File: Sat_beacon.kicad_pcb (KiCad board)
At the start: 2 copper layers, 8 x 3.6 mm, 127 parts, among them IC1 LMX2581ESQE_NOPB, IC2 LMX2581ESQE_NOPB, J1 Conn_01x05_Pin, J2 Conn_01x05_Pin, J3 Conn_01x03_Pin, J4 MMCX, J5 MMCX, Q1 BC817-40, Q2 BC817-40, Q3 BC817-40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

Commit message: PCB work
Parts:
- removed C50, C59: 4.7u, Capacitor_SMD:C_0805_2012Metric
- moved U5 293.2 mm to (99.8, 151.4), turned to 180 degrees
- moved J5 288.3 mm to (100.8, 160.4), turned to 90 degrees
- moved C65 286.6 mm to (95.3, 145.8), turned to 180 degrees
- moved C66 283.0 mm to (99.1, 148.2), turned to -90 degrees
- moved C67 280.8 mm to (100.8, 148.2), turned to -90 degrees
- moved C68 276.3 mm to (104.4, 145.8)
- moved IC2 274.2 mm to (98.8, 132.1)
- moved R22 266.2 mm to (98.9, 117.9)
- moved R20 255.6 mm to (85.9, 134.7)
- moved C24 255.5 mm to (91.3, 130.3)
- moved C45 255.5 mm to (96.6, 139.2)
- moved C42 255.1 mm to (93.7, 124.3), turned to -90 degrees
- moved C60 252.7 mm to (102.3, 124.5), turned to -90 degrees
- moved R21 252.1 mm to (89.3, 136.7)
- moved C47 242.4 mm to (85.9, 136.7)
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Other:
- board size 8 x 3.6 mm -> 3.6 x 8 mm

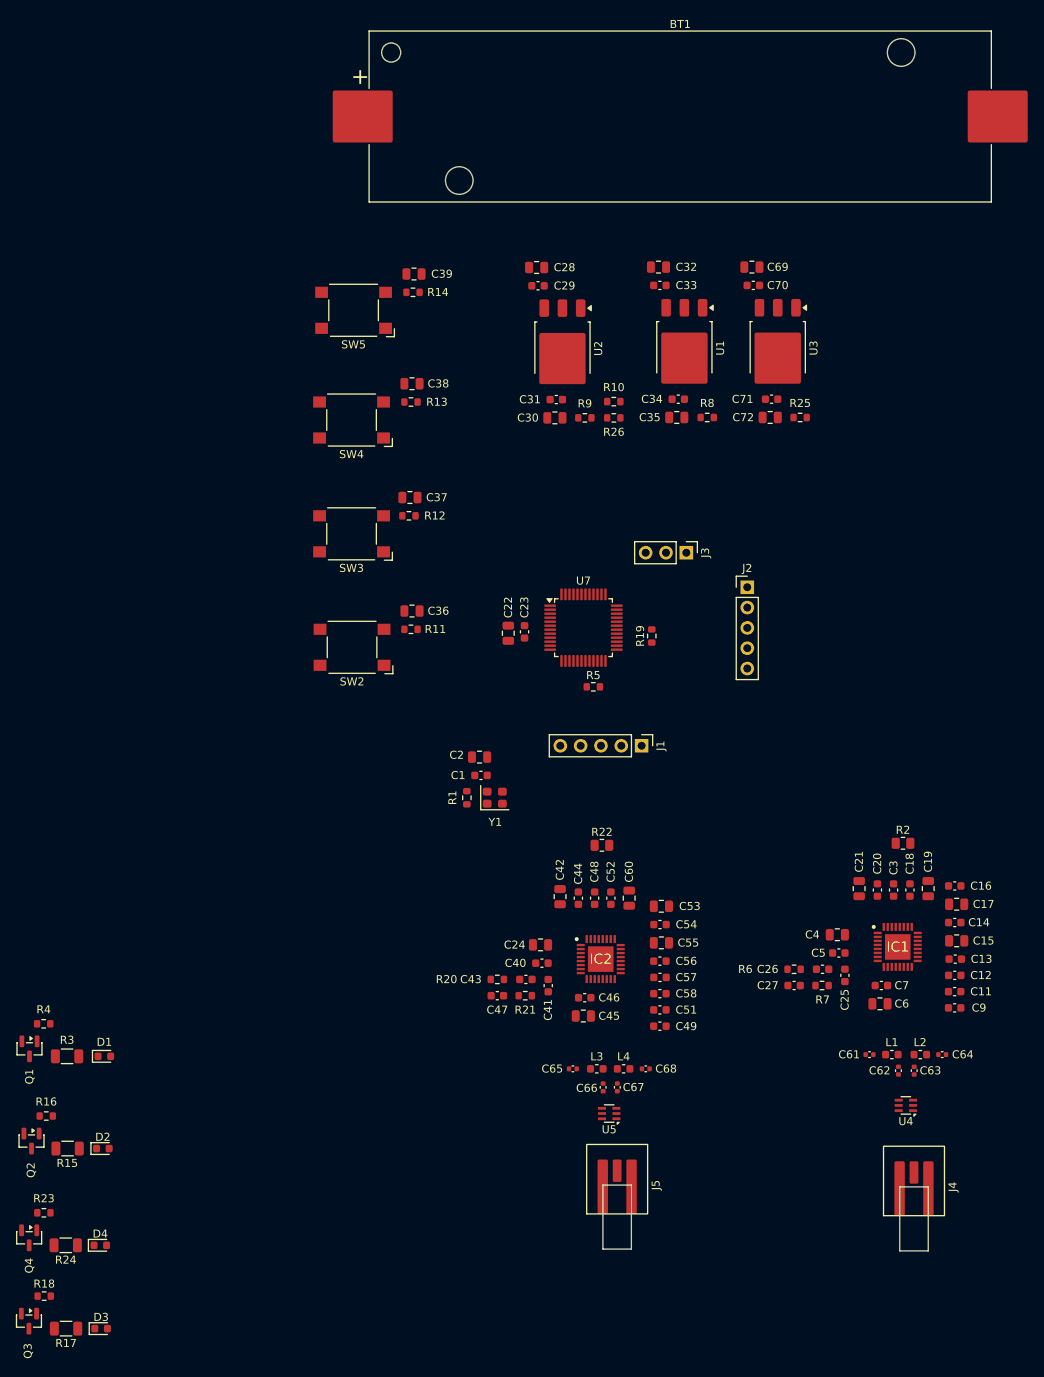
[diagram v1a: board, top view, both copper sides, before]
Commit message: PCB stackup and rules defined, some PCB work done
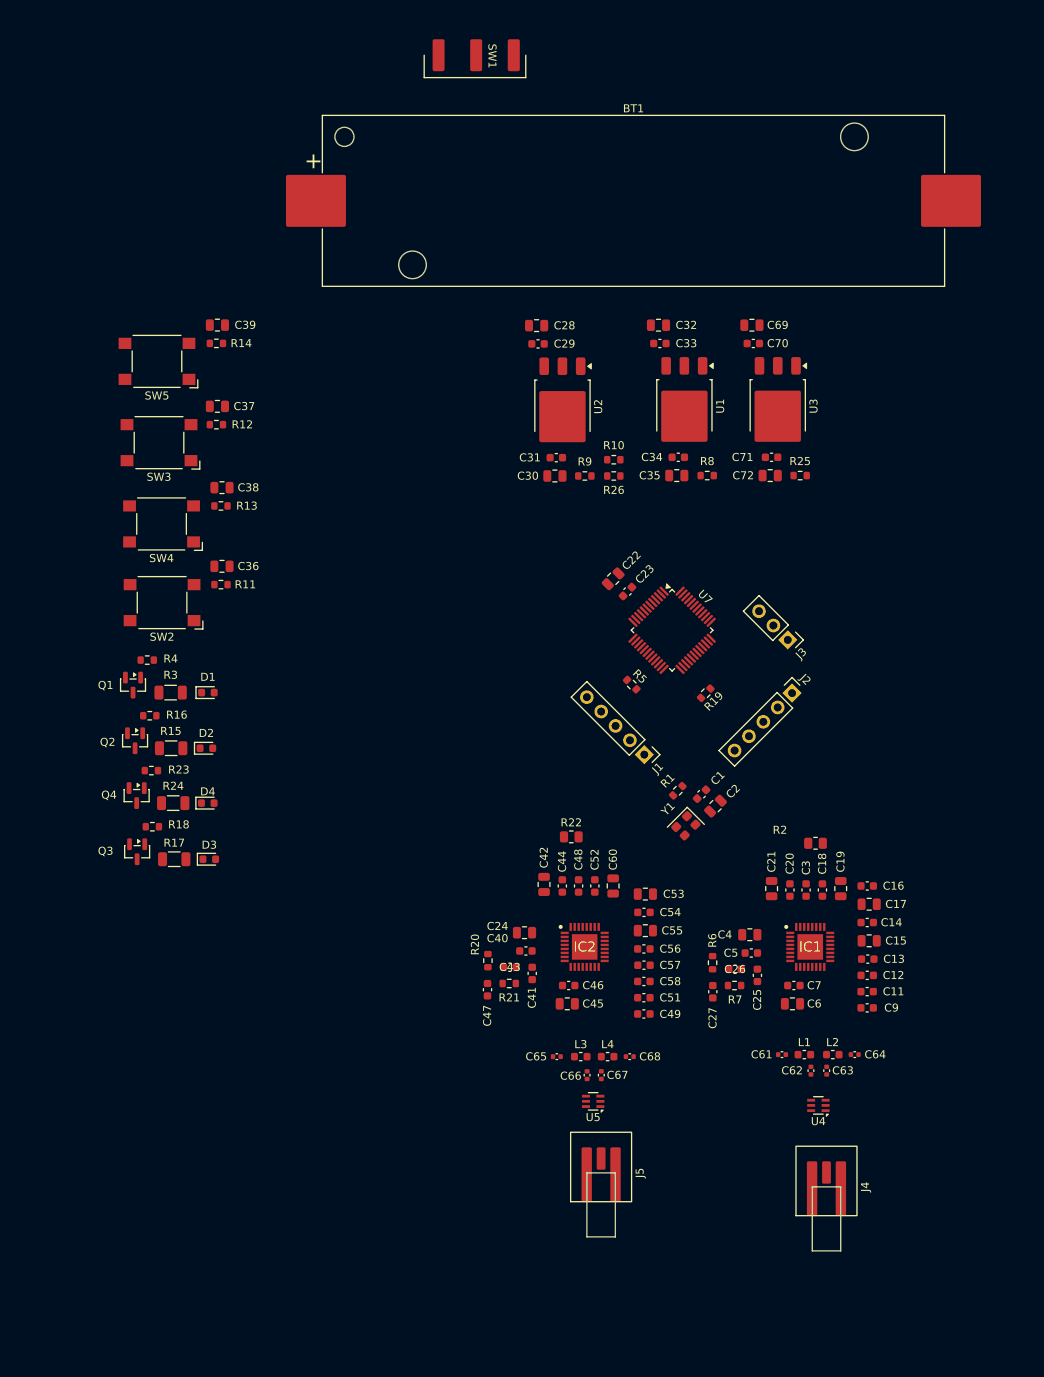
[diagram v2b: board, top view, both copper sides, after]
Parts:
- added SW1: B1407, Switch_sideways:B1407, F.Cu at (83.2, 19.1)
- R2, R22: value 51 -> 100R
- moved R18 60.2 mm to (42.7, 115.6)
- moved D3 60.2 mm to (49.8, 119.6)
- moved Q3 60.2 mm to (40.8, 118.7)
- moved R17 60.2 mm to (45.5, 119.6)
- moved D4 56.9 mm to (49.7, 112.6)
- moved Q4 56.9 mm to (40.8, 111.7)
- moved R23 56.9 mm to (42.6, 108.6)
- moved R24 56.9 mm to (45.3, 112.6)
- moved D2 51.7 mm to (49.5, 105.8)
- moved Q2 51.7 mm to (40.6, 104.8)
- moved R16 51.7 mm to (42.4, 101.7)
- moved R15 51.7 mm to (45.1, 105.8)
- moved D1 47.3 mm to (49.7, 98.8)
- moved Q1 47.3 mm to (40.3, 97.9)
- moved R3 47.3 mm to (45.0, 98.8)
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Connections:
- IC1 pad 30: unconnected-(IC1-MUXOUT-Pad30) -> /PLL_MUXOUT_1
- IC2 pad 30: unconnected-(IC2-MUXOUT-Pad30) -> /PLL_MUXOUT_2
- U7 pad 13: /PLL_LED_2 -> /PLL_LED_1
- U7 pad 14: /PLL_LED_1 -> /PLL_LED_2
- U7 pad 22: /PLL_RF_EN_2 -> /PLL_MUXout_2
- U7 pad 23: unconnected-(U7-PB11-Pad23) -> /PLL_RF_EN_2
- U7 pad 30: /PLL_CE_1 -> /PLL_MUXout_1
- U7 pad 31: unconnected-(U7-PC7-Pad31) -> /PLL_RF_EN_1

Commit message: PCB work
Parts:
- SW1: footprint Switch_sideways:B1407 -> Switch_sideways:flip_switch
- moved C39 82.3 mm to (126.4, 85.6), turned to 90 degrees
- moved R14 81.1 mm to (127.2, 82.3)
- moved SW5 80.8 mm to (119.4, 84.6)
- moved R11 80.6 mm to (127.2, 58.2)
- moved SW2 80.2 mm to (119.4, 60.5)
- moved C36 78.0 mm to (126.4, 61.5), turned to 90 degrees
- moved R12 77.0 mm to (127.2, 74.2)
- moved C37 76.9 mm to (126.4, 77.5), turned to 90 degrees
- moved R13 76.5 mm to (127.2, 66.1)
- moved SW3 76.3 mm to (119.4, 76.5)
- moved SW4 76.1 mm to (119.4, 68.3)
- moved C38 75.0 mm to (126.4, 69.3), turned to 90 degrees
- moved D3 48.0 mm to (85.4, 87.4)
- moved R18 48.0 mm to (78.0, 83.1)
- moved Q3 48.0 mm to (76.3, 86.4)
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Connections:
- SW1 pad 3: VCC_CHARGER -> +BATT
- U7 pad 10: unconnected-(U7-PF2-Pad10) -> /NRST
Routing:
- net VCC_PLL1: track 0.00 -> 163.1 mm, vias 0 -> 7
- net VCC_MCU: track 0.00 -> 78.1 mm, vias 0 -> 1
- net Net-(SW1-B): track 0.00 -> 68.6 mm
- net /VTUNE_1: track 0.00 -> 40.7 mm, vias 0 -> 2
- net /PLL_CLK_1: track 0.00 -> 40.5 mm
- net /PLL_CE_1: track 0.00 -> 40.5 mm
- net /CLK_10MHZ: track 0.00 -> 39.8 mm, vias 0 -> 2
- net /PLL_DATA_1: track 0.00 -> 39.6 mm
- net /PLL_BTN_1: track 0.00 -> 39.4 mm
- net /PLL_LE_1: track 0.00 -> 39.1 mm
- net /PLL_TOGGLE_1: track 0.00 -> 32.4 mm
- net /PLL_BTN_2: track 0.00 -> 24.7 mm
- net VCC_PLL2: track 0.00 -> 18.2 mm, vias 0 -> 2
- net /PLL_TOGGLE_2: track 0.00 -> 16.8 mm
- net Net-(U1-VO): track 0.00 -> 15.8 mm
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
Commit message: PCB work + MCU pin moves
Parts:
- added J6: Conn_01x04_Pin, Connector_PinHeader_2.54mm:PinHeader_1x04_P2.54mm_Vertical, F.Cu at (118.9, 100.1)
- BT1: footprint Battery:BatteryHolder_Keystone_1042_1x18650 -> Battery:BatteryHolder_MPD_BH-18650-PC
- J2: value Conn_01x05_Pin -> Conn_01x03_Pin; footprint Connector_PinHeader_2.54mm:PinHeader_1x05_P2.54mm_Vertical -> Connector_PinHeader_2.54mm:PinHeader_1x03_P2.54mm_Vertical
- J3: value Conn_01x03_Pin -> Conn_Coaxial; footprint Connector_PinHeader_2.54mm:PinHeader_1x03_P2.54mm_Vertical -> Connector_Coaxial:SMA_Amphenol_132289_EdgeMount
- moved J3 161.0 mm to (3.77, 5.61), turned to 0 degrees
- moved BT1 32.5 mm to (138.3, 37.6), turned to 180 degrees
- moved SW1 18.5 mm to (135.6, 57.6), turned to 90 degrees
- moved J2 12.9 mm to (102.9, 115.3), turned to 90 degrees
- moved C2 6.12 mm to (96.9, 104.8), turned to -90 degrees
- moved C1 5.93 mm to (94.6, 105.0), turned to -90 degrees
- moved R1 5.26 mm to (92.3, 106.6), turned to -90 degrees
- moved R5 2.90 mm to (97.8, 100.1)
- moved Y1 2.72 mm to (96.0, 109.2), turned to -90 degrees
- moved R19 1.57 mm to (107.8, 99.3), turned to 0 degrees
- moved J1 1.56 mm to (85.9, 114.3)
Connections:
- IC1 pad 1: /PLL_CLK_1 -> /PLL_CLK
- IC1 pad 2: /PLL_DATA_1 -> /PLL_DATA
- IC2 pad 1: /PLL_CLK_2 -> /PLL_CLK
- IC2 pad 2: /PLL_DATA_2 -> /PLL_DATA
- J1 pad 2: /PLL_CLK_2 -> /PLL_CLK
- J1 pad 3: /PLL_DATA_2 -> /PLL_DATA
- J2 pad 2: /PLL_CLK_1 -> /PLL_CE_1
- J2 pad 3: /PLL_DATA_1 -> /PLL_LE_1
- J3 pad 1: GND -> unconnected-(J3-In-Pad1)
- J3 pad 2: /SWDIO -> unconnected-(J3-Ext-Pad2)
- U7 pad 11: unconnected-(U7-PA0-Pad11) -> /PLL_LED_1
- U7 pad 12: unconnected-(U7-PA1-Pad12) -> /PLL_LED_2
- U7 pad 13: /PLL_LED_1 -> /PLL_DATA
- U7 pad 14: /PLL_LED_2 -> unconnected-(U7-PA3-Pad14)
- U7 pad 16: unconnected-(U7-PA5-Pad16) -> /PLL_CLK
- U7 pad 17: unconnected-(U7-PA6-Pad17) -> /PLL_MUXout
- U7 pad 20: /PLL_DATA_2 -> unconnected-(U7-PB1-Pad20)
- U7 pad 21: /PLL_CLK_2 -> unconnected-(U7-PB2-Pad21)
- U7 pad 22: /PLL_MUXout_2 -> /PLL_MUXOUT_2
- U7 pad 23: /PLL_RF_EN_2 -> unconnected-(U7-PB11-Pad23)
- U7 pad 24: unconnected-(U7-PB12-Pad24) -> /PLL_RF_EN_2
- U7 pad 28: /PLL_DATA_1 -> unconnected-(U7-PA8-Pad28)
- U7 pad 29: /PLL_CLK_1 -> /PLL_MUXOUT_1
- U7 pad 30: /PLL_MUXout_1 -> unconnected-(U7-PC6-Pad30)
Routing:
- net /PLL_DATA: track 0.00 -> 87.2 mm, vias 0 -> 2
- net /PLL_CLK: track 0.00 -> 84.0 mm, vias 0 -> 2
- net VCC_MCU: track 78.1 -> 160.8 mm, vias 1 -> 2
- net /LD_1: track 10.5 -> 75.3 mm, vias 0 -> 2
- net /PLL_CLK_1: track 40.5 -> 0.00 mm
- net /PLL_DATA_1: track 39.6 -> 0.00 mm
- net /NRST: track 0.00 -> 35.9 mm, vias 0 -> 1
- net /PLL_RF_EN_1: track 10.4 -> 45.2 mm
- net /PLL_CE_2: track 0.00 -> 34.4 mm
- net /PLL_LE_2: track 0.00 -> 32.7 mm
- net /PLL_MUXOUT_1: track 6.86 -> 37.4 mm
- net /PLL_LED_1: track 0.00 -> 29.2 mm, vias 0 -> 2
- net /PLL_LED_2: track 0.00 -> 25.6 mm, vias 0 -> 2
- net /PLL_MUXOUT_2: track 0.00 -> 22.7 mm
- net /PLL_RF_EN_2: track 0.00 -> 21.1 mm
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
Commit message: PCB routed
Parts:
- removed J3: Conn_Coaxial, Connector_Coaxial:SMA_Amphenol_132289_EdgeMount
- moved R22 6.90 mm to (91.1, 119.6), turned to 0 degrees
- moved C24 6.19 mm to (80.8, 129.1)
- moved C40 6.00 mm to (81.0, 131.2)
- moved C44 5.22 mm to (87.1, 123.3)
- moved C42 5.03 mm to (85.1, 123.0)
- moved R20 4.79 mm to (78.2, 132.4)
- moved C43 4.77 mm to (81.0, 133.2)
- moved C47 4.76 mm to (78.2, 136.0)
- moved C41 4.75 mm to (83.8, 133.9)
- moved R21 4.74 mm to (81.0, 135.2)
- moved BT1 4.67 mm to (141.6, 40.9)
- moved SW1 4.55 mm to (138.7, 61.0)
- moved C45 4.54 mm to (88.2, 137.5)
- moved C46 4.54 mm to (88.4, 135.2)
- moved IC2 4.52 mm to (90.4, 130.4)
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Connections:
- IC1 pad 30: /PLL_MUXOUT_1 -> /PLL_MUXOUT
- IC2 pad 30: /PLL_MUXOUT_2 -> /PLL_MUXOUT
- U7 pad 22: /PLL_MUXOUT_2 -> /PLL_MUXOUT
- U7 pad 29: /PLL_MUXOUT_1 -> unconnected-(U7-PA9-Pad29)
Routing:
- net VCC_PLL2: track 18.2 -> 225.1 mm, vias 2 -> 7
- net GND: track 0.20 -> 132.5 mm, vias 0 -> 34
- net /PLL_MUXOUT: track 0.00 -> 82.2 mm, vias 0 -> 3
- net VCC_PLL1: track 163.1 -> 226.7 mm
- net /LD_2: track 2.41 -> 56.1 mm, vias 1 -> 2
- net /PLL_MUXOUT_1: track 37.4 -> 0.00 mm
- net /VTUNE_2: track 0.00 -> 34.9 mm, vias 0 -> 2
- net /PLL_CE_2: track 34.4 -> 58.6 mm
- net /PLL_MUXOUT_2: track 22.7 -> 0.00 mm
- net /PLL_DATA: track 87.2 -> 109.6 mm
- net /PLL_CLK: track 84.0 -> 105.5 mm
- net /PLL_LE_2: track 32.7 -> 53.8 mm
- net /PLL_RF_EN_2: track 21.1 -> 41.1 mm
- net VCC_MCU: track 160.8 -> 176.8 mm, vias 2 -> 3
- net /CLK_10MHZ: track 42.5 -> 54.7 mm
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- added copper zone on B.Cu, net GND
- added copper zone on F.Cu, net GND
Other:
- board size 3.6 x 8 mm -> 79.5 x 122.9 mm
- board text added: "David Manasek/NDE/Bot"
- board text added: "David Manasek/NDE/Top"

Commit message: PCB RF section improvement
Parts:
- moved J5 90.8 mm to (169.2, 104.7), turned to 180 degrees
- moved J4 90.4 mm to (168.3, 74.2), turned to 180 degrees
- moved BT1 86.0 mm to (56.8, 55.6), turned to -90 degrees
- moved U4 80.8 mm to (161.6, 75.2), turned to -90 degrees
- moved U5 80.7 mm to (161.6, 105.7), turned to -90 degrees
- moved C63 77.6 mm to (158.9, 74.2), turned to 0 degrees
- moved C66 77.6 mm to (159.0, 106.7), turned to 0 degrees
- moved C67 76.8 mm to (159.0, 104.7), turned to 0 degrees
- moved C62 76.8 mm to (158.9, 76.2), turned to 0 degrees
- moved C64 76.6 mm to (156.9, 70.7), turned to 90 degrees
- moved C65 76.6 mm to (157.0, 110.3), turned to -90 degrees
- moved C47 75.7 mm to (151.9, 118.9), turned to 180 degrees
- moved L2 75.2 mm to (156.9, 73.4), turned to -90 degrees
- moved L3 75.2 mm to (157.0, 107.5), turned to -90 degrees
- moved L4 73.8 mm to (157.0, 103.9), turned to -90 degrees
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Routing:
- net /RF1_DC_N: track 9.93 -> 11.4 mm
- net /RF1_DC_P: track 9.94 -> 11.4 mm
- net /RF1_N: track 1.33 -> 2.70 mm
- net /RF1_P: track 1.30 -> 2.65 mm
- net Net-(SW1-B): track 86.1 -> 87.4 mm
- net VCC_PLL1: track 226.7 -> 227.2 mm
- added copper zone on F.Cu, net /RF1_DC_N
- added copper zone on F.Cu, net /RF1_DC_P
- added copper zone on F.Cu, net /RF2_DC_N
- added copper zone on F.Cu, net /RF2_DC_P
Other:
- board size 79.5 x 122.9 mm -> 122.9 x 79.5 mm

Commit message: new branch for 4 layer board, PCB updated, MMCX -> SMA
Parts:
- J4, J5: value MMCX -> SMA; footprint Library:MMCX-J-P-X-ST-EM1 -> Connector_Coaxial:SMA_Amphenol_132289_EdgeMount
- moved J5 2.86 mm to (166.3, 104.6), turned to 0 degrees
- moved C56 2.51 mm to (144.0, 95.7)
- moved C14 2.34 mm to (143.8, 65.3)
- moved J4 1.98 mm to (166.4, 74.2), turned to 0 degrees
- moved C15 1.98 mm to (141.7, 65.1)
- moved C55 1.81 mm to (142.0, 95.6)
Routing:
- net VCC_PLL1: track 227.2 -> 167.3 mm, vias 7 -> 9
- net VCC_PLL2: track 225.2 -> 169.2 mm, vias 7 -> 9
- net /RF1_DC_P: track 11.4 -> 9.93 mm
- net /RF1_DC_N: track 11.4 -> 9.97 mm
- net Net-(IC2-VBIASCOMP): track 11.5 -> 10.2 mm
- net Net-(IC1-VBIASCOMP): track 11.5 -> 10.3 mm
- net /RF1_N: track 2.70 -> 1.54 mm
- net /RF1_P: track 2.65 -> 1.55 mm
- net GND: vias 34 -> 58
- added copper zone on In1.Cu, net GND
- added copper zone on In2.Cu, net VCC_PLL1
- added copper zone on In2.Cu, net VCC_PLL2
- removed copper zone on F.Cu, net /RF1_DC_N
- removed copper zone on F.Cu, net /RF1_DC_P
- removed copper zone on F.Cu, net /RF2_DC_N
- removed copper zone on F.Cu, net /RF2_DC_P
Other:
- board size 122.9 x 79.5 mm -> 123.9 x 79.5 mm
- copper layers 2 -> 4
- board text removed: "David Manasek/NDE/Bot"
- board text removed: "David Manasek/NDE/Top"

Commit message: PCB improvements
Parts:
- moved R2 0.16 mm to (133.3, 75.7)
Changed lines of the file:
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@@
 	(footprint "Resistor_SMD:R_0805_2012Metric"
 		(layer "F.Cu")
-		(at 133.297317 75.857676 90)
+		(at 133.297317 75.700677 90)
 		(descr "Resistor SMD 0805 (2012 Metric), square (rectangular) end terminal, IPC-7351 nominal, (Body size source: IPC-SM-782 page 72, https://www.pcb-3d.com/wordpress/wp-content/uploads/ipc-sm-782a_amendment_1_and_2.pdf), generated with kicad-footprint-generator")
 		(tags "resistor")
@@
 	(via
 		(at 124.153317 106.996176)
-		(size 2)
-		(drill 1)
+		(size 0.7)
+		(drill 0.3)
 		(layers "F.Cu" "B.Cu")
 		(free yes)
@@
 	)
 	(segment
-		(start 135.837317 76.516177)
-		(end 135.583317 76.770176)
-		(width 0.6)
-		(layer "F.Cu")
-		(net 4)
-	)
-	(segment
 		(start 127.709317 100.900176)
 		(end 127.201318 100.392177)
@@
 	)
 	(segment
-		(start 135.583317 76.770176)
-		(end 133.297317 76.770176)
-		(width 0.6)
-		(layer "F.Cu")
-		(net 4)
-	)
-	(segment
 		(start 135.925593 106.996176)
 		(end 137.944592 106.996177)
@@
 	)
 	(segment
-		(start 133.297317 76.770176)
-		(end 126.185318 76.770176)
-		(width 0.6)
-		(layer "F.Cu")
-		(net 4)
-	)
-	(segment
 		(start 127.709317 103.948177)
 		(end 127.709317 100.900176)
@@
 	)
 	(segment
-		(start 135.837317 76.516177)
+		(start 126.439317 76.516177)
 		(end 137.856317 76.516177)
 		(width 0.6)
@@
 	)
 	(via
-		(at 126.185318 76.770176)
+		(at 126.439317 76.516177)
 		(size 2)
 		(drill 1)
@@
 	(segment
 		(start 124.153317 98.106177)
-		(end 122.629317 96.582177)
+		(end 124.661317 98.106176)
 		(width 0.6)
 		(layer "B.Cu")
@@
 	(segment
 		(start 122.629317 80.326177)
-		(end 126.185318 76.770176)
+		(end 122.629317 96.582177)
 		(width 0.6)
 		(layer "B.Cu")
@@
 	)
 	(segment
-		(start 122.629317 96.582177)
+		(start 126.439317 76.516177)
 		(end 122.629317 80.326177)
 		(width 0.6)
@@
 	)
 	(segment
-		(start 124.661317 98.106176)
+		(start 122.629317 96.582177)
 		(end 124.153317 98.106177)
 		(width 0.6)
@@
 		(name "$teardrop_padvia$")
 		(hatch none 0.1)
-		(priority 30002)
+		(priority 30003)
 		(attr
 			(teardrop
@@
 		(name "$teardrop_padvia$")
 		(hatch none 0.1)
-		(priority 30001)
+		(priority 30006)
 		(attr
 			(teardrop
@@
 		(name "$teardrop_padvia$")
 		(hatch none 0.1)
-		(priority 30005)
+		(priority 30001)
 		(attr
 			(teardrop
@@
 		(priority 1)
 		(connect_pads yes
-			(clearance 0.2)
+			(clearance 0.6)
 		)
 		(min_thickness 0.3)
@@
 		(polygon
 			(pts
-				(xy 117.549317 102.424177) (xy 117.549317 100.392177) (xy 119.835317 100.392177) (xy 119.835317 102.424177)
+				(xy 117.549317 103.694177) (xy 117.549317 98.614177) (xy 119.835317 98.614177) (xy 119.835317 103.694177)
 			)
 		)
@@
 		(name "$teardrop_padvia$")
 		(hatch none 0.1)
-		(priority 30006)
+		(priority 30005)
 		(attr
 			(teardrop
@@
 		(name "$teardrop_padvia$")
 		(hatch none 0.1)
-		(priority 30003)
+		(priority 30002)
 		(attr
 			(teardrop
@@
 		(name "$teardrop_padvia$")
 		(hatch none 0.1)
-		(priority 30015)
+		(priority 30012)
 		(attr
 			(teardrop
@@
 		(name "$teardrop_padvia$")
 		(hatch none 0.1)
-		(priority 30012)
+		(priority 30015)
 		(attr
 			(teardrop
